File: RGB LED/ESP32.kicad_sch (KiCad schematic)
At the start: 6 parts, among them SW1 SW_SPST, SW2 SW_SPST, U3 ESP32-S3-WROOM-1-N4

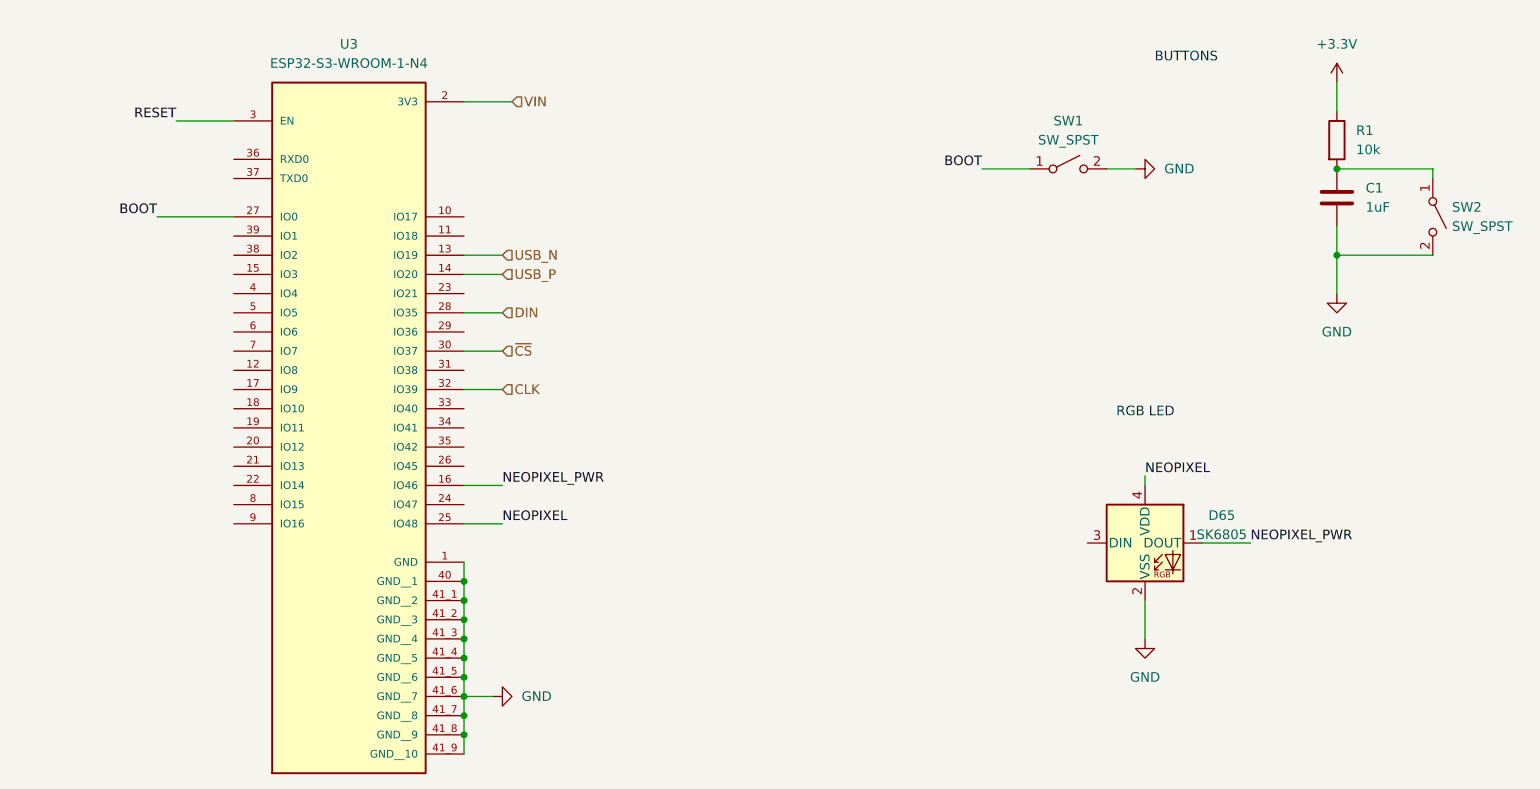
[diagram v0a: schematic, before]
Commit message: edited according to feedback
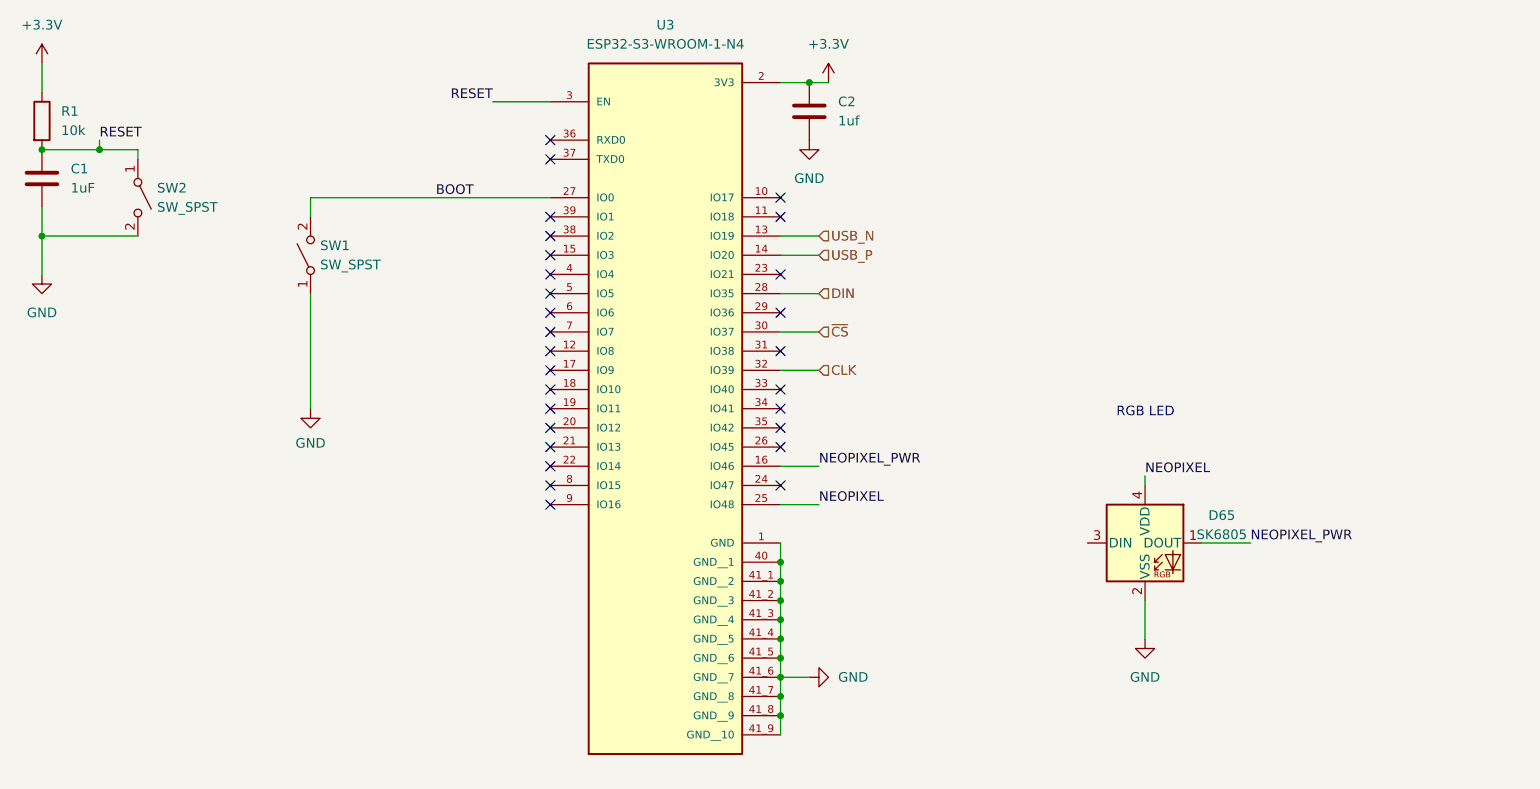
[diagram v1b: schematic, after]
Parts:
- added C2: 1uf, symbol Device:C
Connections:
- net VIN is gone; now on net +3.3V: U3.2 (3V3)
- net +3.3V: now also C2.1
- net BOOT: now also SW1.2 (B); no longer SW1.1 (A)
- net GND: now also SW1.1 (A), C2.2; no longer SW1.2 (B)
- net RESET: now also C1.1, R1.2, SW2.1 (A)
- no-connect marks 0 -> 28
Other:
- note removed: "BUTTONS"
- moved on the sheet: C1, R1, SW1, SW2, U3

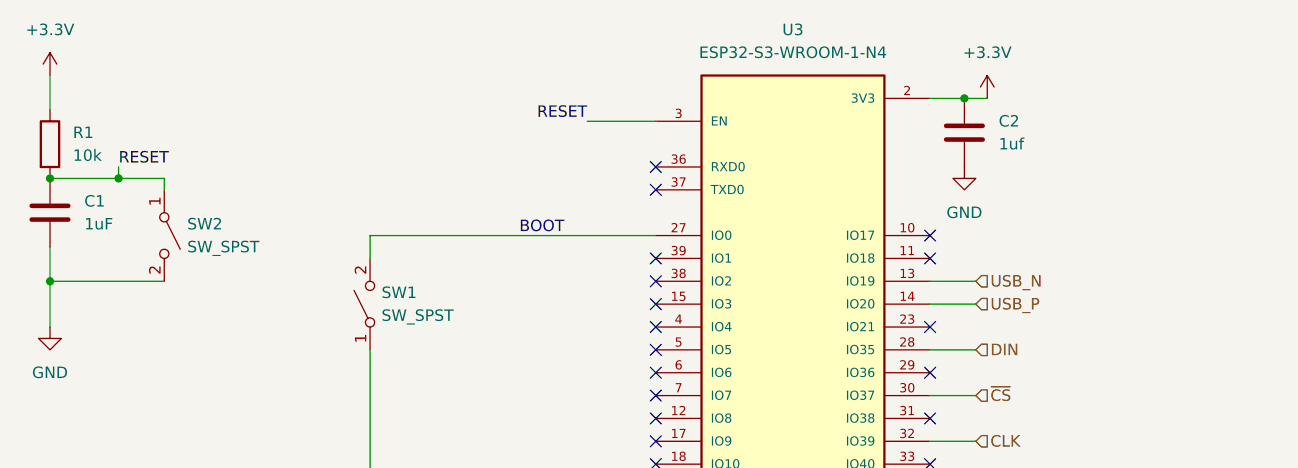
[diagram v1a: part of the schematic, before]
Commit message: added footprints
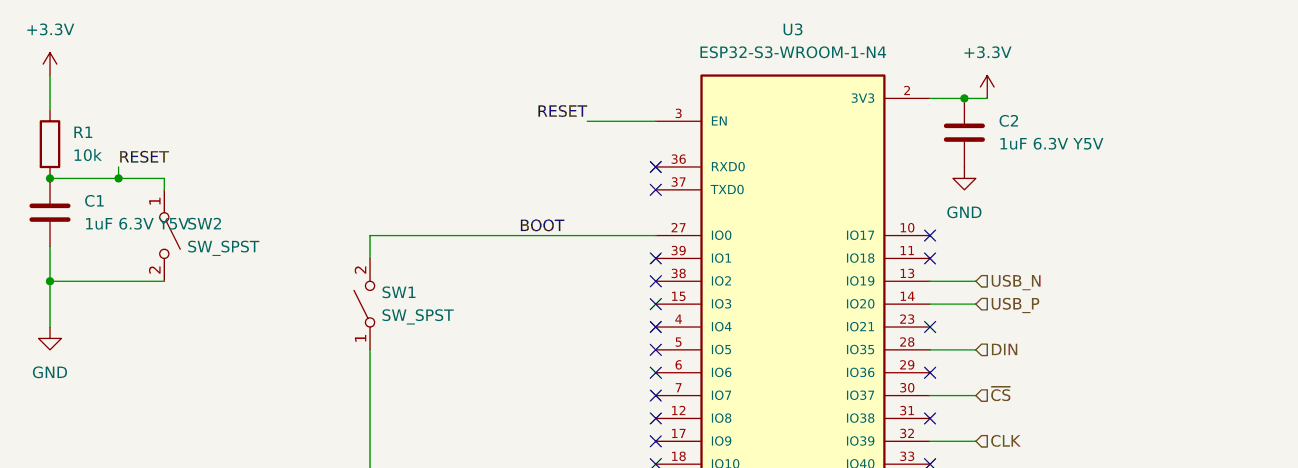
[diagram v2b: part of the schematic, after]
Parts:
- C1: value 1uF -> 1uF 6.3V Y5V; footprint (none) -> Capacitor_SMD:C_0603_1608Metric
- C2: value 1uf -> 1uF 6.3V Y5V; footprint (none) -> Capacitor_SMD:C_0603_1608Metric
- R1: footprint (none) -> Resistor_SMD:R_0603_1608Metric
- SW1, SW2: footprint (none) -> Button_Switch_SMD:SW_SPST_FSMSM
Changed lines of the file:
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@@
       (effects (font (size 1.27 1.27)) (justify left))
     )
-    (property "Footprint" "" (at 43.942 55.88 90)
+    (property "Footprint" "Resistor_SMD:R_0603_1608Metric" (at 43.942 55.88 90)
       (effects (font (size 1.27 1.27)) hide)
     )
@@
       (effects (font (size 1.27 1.27)) (justify left))
     )
-    (property "Value" "1uf" (at 151.13 55.88 0)
-      (effects (font (size 1.27 1.27)) (justify left))
-    )
-    (property "Footprint" "" (at 148.2852 58.42 0)
+    (property "Value" "1uF 6.3V Y5V" (at 151.13 55.88 0)
+      (effects (font (size 1.27 1.27)) (justify left))
+    )
+    (property "Footprint" "Capacitor_SMD:C_0603_1608Metric" (at 148.2852 58.42 0)
       (effects (font (size 1.27 1.27)) hide)
     )
@@
       (effects (font (size 1.27 1.27)) (justify right))
     )
-    (property "Footprint" "" (at 81.28 73.66 0)
+    (property "Footprint" "Button_Switch_SMD:SW_SPST_FSMSM" (at 81.28 73.66 0)
       (effects (font (size 1.27 1.27)) hide)
     )
@@
       (effects (font (size 1.27 1.27)) (justify left))
     )
-    (property "Footprint" "" (at 58.42 66.04 0)
+    (property "Footprint" "Button_Switch_SMD:SW_SPST_FSMSM" (at 58.42 66.04 0)
       (effects (font (size 1.27 1.27)) hide)
     )
@@
       (effects (font (size 1.27 1.27)) (justify left))
     )
-    (property "Value" "1uF" (at 49.53 64.77 0)
-      (effects (font (size 1.27 1.27)) (justify left))
-    )
-    (property "Footprint" "" (at 46.6852 67.31 0)
-      (effects (font (size 1.27 1.27)) hide)
-    )
+    (property "Value" "1uF 6.3V Y5V" (at 49.53 64.77 0)
+      (effects (font (size 1.27 1.27)) (justify left))
+    )
+    (property "Footprint" "Capacitor_SMD:C_0603_1608Metric" (at 46.6852 67.31 0)
+      (effects (font (size 1.27 1.27)) hide)
+    )

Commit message: started layout
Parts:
- R1: value 10k -> 5.1K 1%
- SW1, SW2: value SW_SPST -> SW_SPST_FSMSM
- U3: footprint ESP32-S3-WROOM-1-N4:XCVR_ESP32-S3-WROOM-1-N4 -> Library:XCVR_ESP32-S3-WROOM-1-N4
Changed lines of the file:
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@@
       (effects (font (size 1.27 1.27)) (justify left))
     )
-    (property "Value" "10k" (at 48.26 57.15 0)
+    (property "Value" "5.1K 1%" (at 48.26 57.15 0)
       (effects (font (size 1.27 1.27)) (justify left))
     )
@@
       (effects (font (size 1.27 1.27)))
     )
-    (property "Footprint" "ESP32-S3-WROOM-1-N4:XCVR_ESP32-S3-WROOM-1-N4" (at 128.27 81.28 0)
+    (property "Footprint" "Library:XCVR_ESP32-S3-WROOM-1-N4" (at 128.27 81.28 0)
       (effects (font (size 1.27 1.27)) (justify bottom) hide)
     )
@@
       (effects (font (size 1.27 1.27)) (justify right))
     )
-    (property "Value" "SW_SPST" (at 82.55 74.93 90)
+    (property "Value" "SW_SPST_FSMSM" (at 82.55 74.93 90)
       (effects (font (size 1.27 1.27)) (justify right))
     )
@@
       (effects (font (size 1.27 1.27)) (justify left))
     )
-    (property "Value" "SW_SPST" (at 60.96 67.31 90)
-      (effects (font (size 1.27 1.27)) (justify left))
-    )
+    (property "Value" "SW_SPST_FSMSM" (at 60.96 67.31 90)
+      (effects (font (size 1.27 1.27)) (justify left))
+    )

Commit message: schematic edits
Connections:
- net NEOPIXEL: now also D65.3 (DIN); no longer D65.4 (VDD)
- net NEOPIXEL_PWR: now also D65.4 (VDD); no longer D65.1 (DOUT)
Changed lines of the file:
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@@
     (stroke (width 0) (type default))
   )
-  (wire (pts (xy 199.39 111.76) (xy 205.74 111.76))
+  (wire (pts (xy 180.34 111.76) (xy 184.15 111.76))
     (stroke (width 0) (type default))
   )
@@
     (effects (font (size 1.27 1.27)) (justify right bottom))
   )
-  (label "NEOPIXEL_PWR" (at 205.74 111.76 0) (fields_autoplaced)
-    (effects (font (size 1.27 1.27)) (justify left bottom))
-  )
   (label "BOOT" (at 102.87 66.04 180) (fields_autoplaced)
     (effects (font (size 1.27 1.27)) (justify right bottom))
   )
-  (label "NEOPIXEL" (at 191.77 102.87 0) (fields_autoplaced)
+  (label "NEOPIXEL_PWR" (at 191.77 102.87 0) (fields_autoplaced)
     (effects (font (size 1.27 1.27)) (justify left bottom))
   )
@@
     (effects (font (size 1.27 1.27)) (justify left bottom))
   )
+  (label "NEOPIXEL" (at 180.34 111.76 180) (fields_autoplaced)
+    (effects (font (size 1.27 1.27)) (justify right bottom))
+  )
   (hierarchical_label "USB_N" (shape input) (at 148.59 71.12 0) (fields_autoplaced)

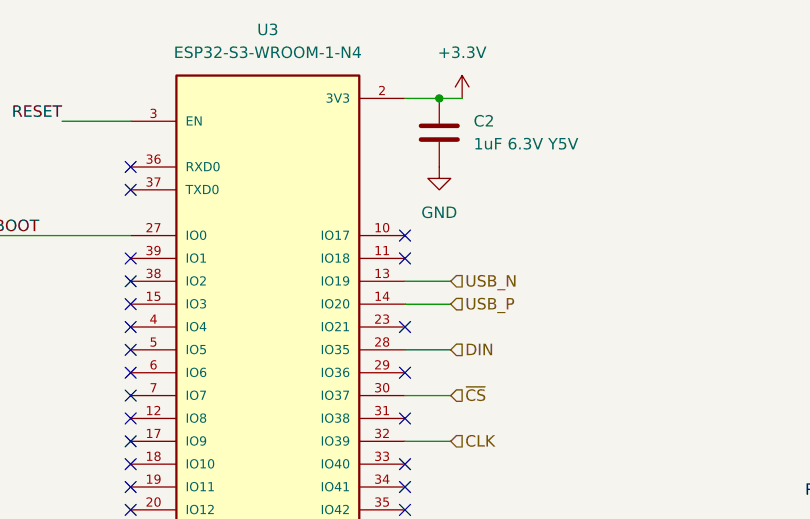
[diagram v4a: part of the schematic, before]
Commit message: changed layout, added traces/vias
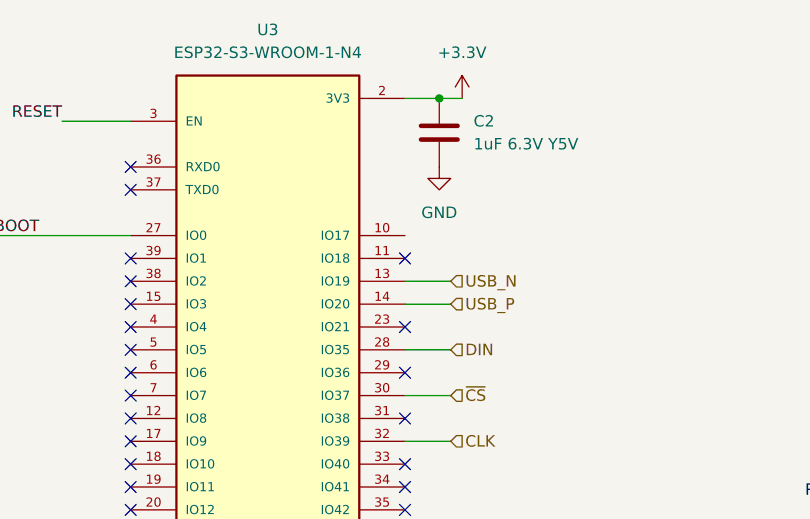
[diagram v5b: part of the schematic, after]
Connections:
- no-connect marks 28 -> 27
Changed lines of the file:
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@@
   (no_connect (at 113.03 60.96))
   (no_connect (at 143.51 91.44))
-  (no_connect (at 143.51 66.04))
   (no_connect (at 113.03 78.74))
   (no_connect (at 113.03 93.98))
